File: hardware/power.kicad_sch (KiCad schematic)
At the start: 0 parts

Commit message: power.kicad_sch düzenlemesi yapıldı.
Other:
- added sheet Filter (power_filter.kicad_sch)
- added sheet Power 12V (power_12v.kicad_sch)
- added sheet Power 3V3 (power_3v3.kicad_sch)
- added sheet Power 5V (power_5v.kicad_sch)
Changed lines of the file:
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@@
 (kicad_sch (version 20230121) (generator eeschema)
   (paper "A4")
+  (wire (pts (xy 93.98 49.53) (xy 118.11 49.53))
+    (stroke (width 0) (type default))
+  )
+  (wire (pts (xy 212.09 76.2) (xy 232.41 76.2))
+    (stroke (width 0) (type default))
+  )
+  (wire (pts (xy 212.09 46.99) (xy 232.41 46.99))
+    (stroke (width 0) (type default))
+  )
+  (wire (pts (xy 50.8 46.99) (xy 58.42 46.99))
+    (stroke (width 0) (type default))
+  )
+  (wire (pts (xy 212.09 78.74) (xy 232.41 78.74))
+    (stroke (width 0) (type default))
+  )
+  (wire (pts (xy 177.8 46.99) (xy 157.48 46.99))
+    (stroke (width 0) (type default))
+  )
+  (wire (pts (xy 212.09 49.53) (xy 232.41 49.53))
+    (stroke (width 0) (type default))
+  )
+  (wire (pts (xy 50.8 49.53) (xy 58.42 49.53))
+    (stroke (width 0) (type default))
+  )
+  (wire (pts (xy 93.98 46.99) (xy 118.11 46.99))
+    (stroke (width 0) (type default))
+  )
+  (wire (pts (xy 177.8 49.53) (xy 157.48 49.53))
+    (stroke (width 0) (type default))
+  )
+  (label "PWR_SOURCE_GND" (at 212.09 78.74 0) (fields_autoplaced)
+    (effects (font (size 1.27 1.27)) (justify left bottom))
+  )
+  (label "PWR_SOURCE_VCC" (at 212.09 46.99 0) (fields_autoplaced)
+    (effects (font (size 1.27 1.27)) (justify left bottom))
+  )
+  (label "PWR_SOURCE_VCC" (at 177.8 46.99 180) (fields_autoplaced)
+    (effects (font (size 1.27 1.27)) (justify right bottom))
+  )
+  (label "PWR_SOURCE_GND" (at 212.09 49.53 0) (fields_autoplaced)
+    (effects (font (size 1.27 1.27)) (justify left bottom))
+  )
+  (label "PWR_SOURCE_GND" (at 177.8 49.53 180) (fields_autoplaced)
+    (effects (font (size 1.27 1.27)) (justify right bottom))
+  )
+  (label "PWR_SOURCE_VCC" (at 212.09 76.2 0) (fields_autoplaced)
+    (effects (font (size 1.27 1.27)) (justify left bottom))
+  )
+  (hierarchical_label "PWR_GND" (shape output) (at 50.8 49.53 180) (fields_autoplaced)
+    (effects (font (size 1.27 1.27)) (justify right))
+  )
+  (hierarchical_label "PWR_VCC" (shape input) (at 50.8 46.99 180) (fields_autoplaced)
+    (effects (font (size 1.27 1.27)) (justify right))
+  )
+  (sheet (at 58.42 44.45) (size 35.56 20.32) (fields_autoplaced)
+    (stroke (width 0.1524) (type solid))
+    (fill (color 0 0 0 0.0000))
+    (property "Sheetname" "Filter" (at 58.42 43.7384 0)
+      (effects (font (size 1.27 1.27)) (justify left bottom))
+    )
+    (property "Sheetfile" "power_filter.kicad_sch" (at 58.42 65.3546 0)
+      (effects (font (size 1.27 1.27)) (justify left top))
+    )
+    (pin "PWR_GND" output (at 58.42 49.53 180)
+      (effects (font (size 1.27 1.27)) (justify left))
+    )
+    (pin "PWR_VCC" input (at 58.42 46.99 180)
+      (effects (font (size 1.27 1.27)) (justify left))
+    )
+    (pin "PWR_SOURCE_VCC" output (at 93.98 46.99 0)
+      (effects (font (size 1.27 1.27)) (justify right))
+    )
+    (pin "PWR_SOURCE_GND" input (at 93.98 49.53 0)
+      (effects (font (size 1.27 1.27)) (justify right))
+    )
+    (instances
+      (project "drip-irrigation-sys-cc"
+        (path "/41708c1e-19b2-4374-83f2-108076d82b45/4f778b49-8d1a-4c8f-a914-ecde21a56ebf" (page "9"))
+      )
+    )
+  )
+  (sheet (at 232.41 44.45) (size 39.37 20.32) (fields_autoplaced)
+    (stroke (width 0.1524) (type solid))
+    (fill (color 0 0 0 0.0000))
+    (property "Sheetname" "Power 5V" (at 232.41 43.7384 0)
+      (effects (font (size 1.27 1.27)) (justify left bottom))
+    )
+    (property "Sheetfile" "power_5v.kicad_sch" (at 232.41 65.3546 0)
+      (effects (font (size 1.27 1.27)) (justify left top))
+    )
+    (pin "PWR_SOURCE_GND" input (at 232.41 49.53 180)
+      (effects (font (size 1.27 1.27)) (justify left))
+    )
+    (pin "PWR_SOURCE_VCC" output (at 232.41 46.99 180)
+      (effects (font (size 1.27 1.27)) (justify left))
+    )
+    (instances
+      (project "drip-irrigation-sys-cc"
+        (path "/41708c1e-19b2-4374-83f2-108076d82b45/4f778b49-8d1a-4c8f-a914-ecde21a56ebf" (page "11"))
+      )
+    )
+  )
+  (sheet (at 232.41 73.66) (size 39.37 21.59) (fields_autoplaced)
+    (stroke (width 0.1524) (type solid))
+    (fill (color 0 0 0 0.0000))
+    (property "Sheetname" "Power 3V3" (at 232.41 72.9484 0)
+      (effects (font (size 1.27 1.27)) (justify left bottom))
+    )
+    (property "Sheetfile" "power_3v3.kicad_sch" (at 232.41 95.8346 0)
+      (effects (font (size 1.27 1.27)) (justify left top))
+    )
+    (pin "PWR_SOURCE_GND" input (at 232.41 78.74 180)
+      (effects (font (size 1.27 1.27)) (justify left))
+    )
+    (pin "PWR_SOURCE_VCC" output (at 232.41 76.2 180)
+      (effects (font (size 1.27 1.27)) (justify left))
+    )
+    (instances
+      (project "drip-irrigation-sys-cc"
+        (path "/41708c1e-19b2-4374-83f2-108076d82b45/4f778b49-8d1a-4c8f-a914-ecde21a56ebf" (page "10"))
+      )
+    )
+  )
+  (sheet (at 118.11 44.45) (size 39.37 20.32) (fields_autoplaced)
+    (stroke (width 0.1524) (type solid))
+    (fill (color 0 0 0 0.0000))
+    (property "Sheetname" "Power 12V" (at 118.11 43.7384 0)
+      (effects (font (size 1.27 1.27)) (justify left bottom))
+    )
+    (property "Sheetfile" "power_12v.kicad_sch" (at 118.11 65.3546 0)
+      (effects (font (size 1.27 1.27)) (justify left top))
+    )
+    (pin "PWR_SOURCE_GND" input (at 118.11 49.53 180)
+      (effects (font (size 1.27 1.27)) (justify left))
+    )
+    (pin "PWR_SOURCE_VCC" output (at 118.11 46.99 180)
+      (effects (font (size 1.27 1.27)) (justify left))
+    )
+    (pin "PWR_12V" output (at 157.48 46.99 0)
+      (effects (font (size 1.27 1.27)) (justify right))
+    )
+    (pin "PWR_12V_GND" output (at 157.48 49.53 0)
+      (effects (font (size 1.27 1.27)) (justify right))
+    )
+    (instances
+      (project "drip-irrigation-sys-cc"
+        (path "/41708c1e-19b2-4374-83f2-108076d82b45/4f778b49-8d1a-4c8f-a914-ecde21a56ebf" (page "12"))
+      )
+    )
+  )
 )

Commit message: Kicad şema düzenlemesi yapıldı.
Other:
- sheet Power 3V3 ports: added GND_3.3V, VCC_3.3V; removed none
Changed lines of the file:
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@@
       (effects (font (size 1.27 1.27)) (justify left))
+    )
+    (pin "VCC_3.3V" input (at 271.78 76.2 0)
+      (effects (font (size 1.27 1.27)) (justify right))
+    )
+    (pin "GND_3.3V" input (at 271.78 78.74 0)
+      (effects (font (size 1.27 1.27)) (justify right))
     )
     (instances

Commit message: Kicad şema düzenlemesi yapıldı.
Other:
- sheet Power 12V ports: added none; removed PWR_12V, PWR_12V_GND
- sheet Power 3V3 ports: added none; removed GND_3.3V, PWR_SOURCE_GND, PWR_SOURCE_VCC, VCC_3.3V
- sheet Power 5V ports: added none; removed PWR_SOURCE_GND, PWR_SOURCE_VCC
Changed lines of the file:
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@@
-    (stroke (width 0) (type default))
-  )
-  (wire (pts (xy 212.09 76.2) (xy 232.41 76.2))
-    (stroke (width 0) (type default))
-  )
-  (wire (pts (xy 212.09 46.99) (xy 232.41 46.99))
     (stroke (width 0) (type default))
   )
   (wire (pts (xy 50.8 46.99) (xy 58.42 46.99))
-    (stroke (width 0) (type default))
-  )
-  (wire (pts (xy 212.09 78.74) (xy 232.41 78.74))
-    (stroke (width 0) (type default))
-  )
-  (wire (pts (xy 177.8 46.99) (xy 157.48 46.99))
-    (stroke (width 0) (type default))
-  )
-  (wire (pts (xy 212.09 49.53) (xy 232.41 49.53))
     (stroke (width 0) (type default))
   )
@@
   (wire (pts (xy 93.98 46.99) (xy 118.11 46.99))
     (stroke (width 0) (type default))
-  )
-  (wire (pts (xy 177.8 49.53) (xy 157.48 49.53))
-    (stroke (width 0) (type default))
-  )
-  (label "PWR_SOURCE_GND" (at 212.09 78.74 0) (fields_autoplaced)
-    (effects (font (size 1.27 1.27)) (justify left bottom))
-  )
-  (label "PWR_SOURCE_VCC" (at 212.09 46.99 0) (fields_autoplaced)
-    (effects (font (size 1.27 1.27)) (justify left bottom))
-  )
-  (label "PWR_SOURCE_VCC" (at 177.8 46.99 180) (fields_autoplaced)
-    (effects (font (size 1.27 1.27)) (justify right bottom))
-  )
-  (label "PWR_SOURCE_GND" (at 212.09 49.53 0) (fields_autoplaced)
-    (effects (font (size 1.27 1.27)) (justify left bottom))
-  )
-  (label "PWR_SOURCE_GND" (at 177.8 49.53 180) (fields_autoplaced)
-    (effects (font (size 1.27 1.27)) (justify right bottom))
-  )
-  (label "PWR_SOURCE_VCC" (at 212.09 76.2 0) (fields_autoplaced)
-    (effects (font (size 1.27 1.27)) (justify left bottom))
   )
   (hierarchical_label "PWR_GND" (shape output) (at 50.8 49.53 180) (fields_autoplaced)
@@
       (effects (font (size 1.27 1.27)) (justify left top))
     )
-    (pin "PWR_SOURCE_GND" input (at 232.41 49.53 180)
-      (effects (font (size 1.27 1.27)) (justify left))
-    )
-    (pin "PWR_SOURCE_VCC" output (at 232.41 46.99 180)
-      (effects (font (size 1.27 1.27)) (justify left))
-    )
     (instances
       (project "drip-irrigation-sys-cc"
@@
     (property "Sheetfile" "power_3v3.kicad_sch" (at 232.41 95.8346 0)
       (effects (font (size 1.27 1.27)) (justify left top))
-    )
-    (pin "PWR_SOURCE_GND" input (at 232.41 78.74 180)
-      (effects (font (size 1.27 1.27)) (justify left))
-    )
-    (pin "PWR_SOURCE_VCC" output (at 232.41 76.2 180)
-      (effects (font (size 1.27 1.27)) (justify left))
-    )
-    (pin "VCC_3.3V" input (at 271.78 76.2 0)
-      (effects (font (size 1.27 1.27)) (justify right))
-    )
-    (pin "GND_3.3V" input (at 271.78 78.74 0)
-      (effects (font (size 1.27 1.27)) (justify right))
     )
     (instances
@@
       (effects (font (size 1.27 1.27)) (justify left))
     )
-    (pin "PWR_12V" output (at 157.48 46.99 0)
-      (effects (font (size 1.27 1.27)) (justify right))
-    )
-    (pin "PWR_12V_GND" output (at 157.48 49.53 0)
-      (effects (font (size 1.27 1.27)) (justify right))
-    )
     (instances

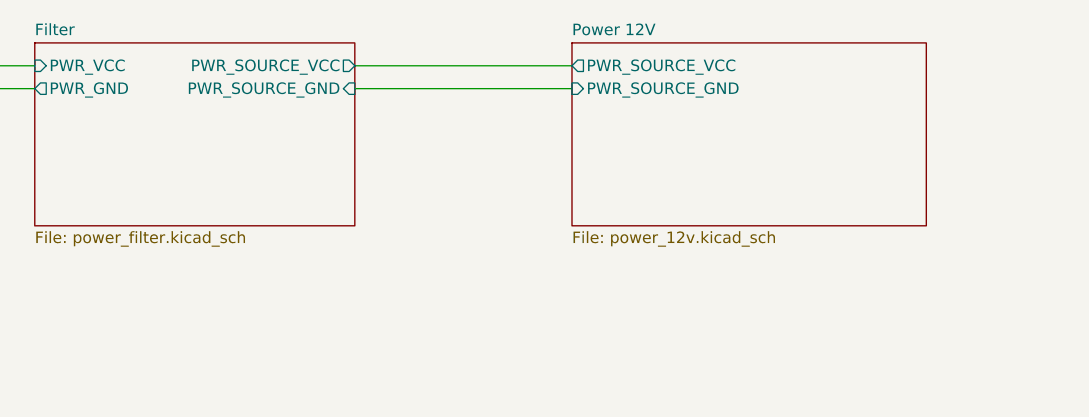
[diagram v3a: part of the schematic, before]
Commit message: Kicad Power Modülü Tamamlandı.
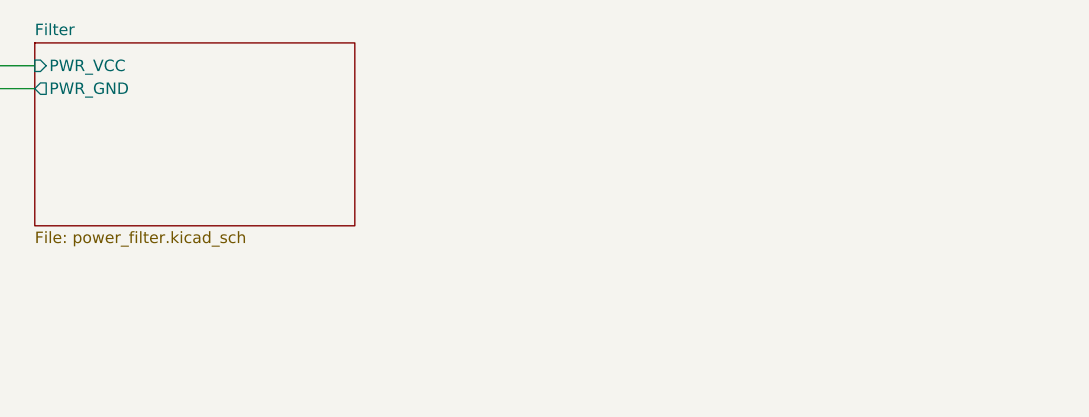
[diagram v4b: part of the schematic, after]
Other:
- removed sheet Power 12V
- sheet Filter ports: added none; removed PWR_SOURCE_GND, PWR_SOURCE_VCC
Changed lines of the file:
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@@
 (kicad_sch (version 20230121) (generator eeschema)
   (paper "A4")
-  (wire (pts (xy 93.98 49.53) (xy 118.11 49.53))
-    (stroke (width 0) (type default))
-  )
   (wire (pts (xy 50.8 46.99) (xy 58.42 46.99))
     (stroke (width 0) (type default))
   )
   (wire (pts (xy 50.8 49.53) (xy 58.42 49.53))
-    (stroke (width 0) (type default))
-  )
-  (wire (pts (xy 93.98 46.99) (xy 118.11 46.99))
     (stroke (width 0) (type default))
   )
@@
     (pin "PWR_VCC" input (at 58.42 46.99 180)
       (effects (font (size 1.27 1.27)) (justify left))
-    )
-    (pin "PWR_SOURCE_VCC" output (at 93.98 46.99 0)
-      (effects (font (size 1.27 1.27)) (justify right))
-    )
-    (pin "PWR_SOURCE_GND" input (at 93.98 49.53 0)
-      (effects (font (size 1.27 1.27)) (justify right))
     )
     (instances
@@
       )
     )
-  )
-  (sheet (at 118.11 44.45) (size 39.37 20.32) (fields_autoplaced)
-    (stroke (width 0.1524) (type solid))
-    (fill (color 0 0 0 0.0000))
-    (property "Sheetname" "Power 12V" (at 118.11 43.7384 0)
-      (effects (font (size 1.27 1.27)) (justify left bottom))
-    )
-    (property "Sheetfile" "power_12v.kicad_sch" (at 118.11 65.3546 0)
-      (effects (font (size 1.27 1.27)) (justify left top))
-    )
-    (pin "PWR_SOURCE_GND" input (at 118.11 49.53 180)
-      (effects (font (size 1.27 1.27)) (justify left))
-    )
-    (pin "PWR_SOURCE_VCC" output (at 118.11 46.99 180)
-      (effects (font (size 1.27 1.27)) (justify left))
-    )
-    (instances
-      (project "drip-irrigation-sys-cc"
-        (path "/41708c1e-19b2-4374-83f2-108076d82b45/4f778b49-8d1a-4c8f-a914-ecde21a56ebf" (page "12"))
-      )
-    )

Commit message: Kicad şema düzenlemesi yapıldı.
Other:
- added sheet 4V (4v.kicad_sch)
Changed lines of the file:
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@@
+    )
+  )
+  (sheet (at 232.41 106.68) (size 39.37 22.86) (fields_autoplaced)
+    (stroke (width 0.1524) (type solid))
+    (fill (color 0 0 0 0.0000))
+    (property "Sheetname" "4V" (at 232.41 105.9684 0)
+      (effects (font (size 1.27 1.27)) (justify left bottom))
+    )
+    (property "Sheetfile" "4v.kicad_sch" (at 232.41 130.1246 0)
+      (effects (font (size 1.27 1.27)) (justify left top))
+    )
+    (instances
+      (project "drip-irrigation-sys-cc"
+        (path "/41708c1e-19b2-4374-83f2-108076d82b45/4f778b49-8d1a-4c8f-a914-ecde21a56ebf" (page "12"))
+      )
     )
   )

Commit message: Kicad düzenleme.
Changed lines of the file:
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@@
+    (stroke (width 0) (type default))
+  )
+  (wire (pts (xy 266.7 21.59) (xy 278.13 21.59))
     (stroke (width 0) (type default))
   )
@@
     (effects (font (size 1.27 1.27)) (justify right))
   )
+  (hierarchical_label "5V" (shape output) (at 278.13 21.59 0) (fields_autoplaced)
+    (effects (font (size 1.27 1.27)) (justify left))
+  )
   (hierarchical_label "PWR_VCC" (shape input) (at 50.8 46.99 180) (fields_autoplaced)
     (effects (font (size 1.27 1.27)) (justify right))
   )
+  (symbol (lib_id "power:+5V") (at 266.7 21.59 0) (unit 1)
+    (in_bom yes) (on_board yes) (dnp no) (fields_autoplaced)
+    (property "Reference" "#PWR017" (at 266.7 25.4 0)
+      (effects (font (size 1.27 1.27)) hide)
+    )
+    (property "Value" "+5V" (at 266.7 16.51 0)
+      (effects (font (size 1.27 1.27)))
+    )
+    (property "Footprint" "" (at 266.7 21.59 0)
+      (effects (font (size 1.27 1.27)) hide)
+    )
+    (property "Datasheet" "" (at 266.7 21.59 0)
+      (effects (font (size 1.27 1.27)) hide)
+    )
+    (pin "1")
+    (instances
+      (project "drip-irrigation-sys-cc"
+        (path "/41708c1e-19b2-4374-83f2-108076d82b45/4f778b49-8d1a-4c8f-a914-ecde21a56ebf"
+          (reference "#PWR017") (unit 1)
+        )
+      )
+    )
+  )
   (sheet (at 58.42 44.45) (size 35.56 20.32) (fields_autoplaced)

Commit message: Kicad şema düzenlemesi yapıldı.
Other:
- removed sheet 4V
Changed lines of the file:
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@@
-    )
-  )
-  (sheet (at 232.41 106.68) (size 39.37 22.86) (fields_autoplaced)
-    (stroke (width 0.1524) (type solid))
-    (fill (color 0 0 0 0.0000))
-    (property "Sheetname" "4V" (at 232.41 105.9684 0)
-      (effects (font (size 1.27 1.27)) (justify left bottom))
-    )
-    (property "Sheetfile" "4v.kicad_sch" (at 232.41 130.1246 0)
-      (effects (font (size 1.27 1.27)) (justify left top))
-    )
-    (instances
-      (project "drip-irrigation-sys-cc"
-        (path "/41708c1e-19b2-4374-83f2-108076d82b45/4f778b49-8d1a-4c8f-a914-ecde21a56ebf" (page "12"))
-      )
     )
   )
